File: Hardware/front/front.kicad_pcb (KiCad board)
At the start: 4 copper layers, 75 x 60 mm, 55 parts, among them J101 Conn_02x10_Odd_Even, SW101 Alps EC11E, SW102 C&K-D6R-Illuminated, SW103 B3W-9002-Y1C, SW104 B3W-9002-Y1C, SW105 B3W-9002-Y1C, SW106 B3W-9002-Y1C, SW107 B3W-9000-RHG2C, U101 XRA1203, U102 AT24CS32-SSHM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

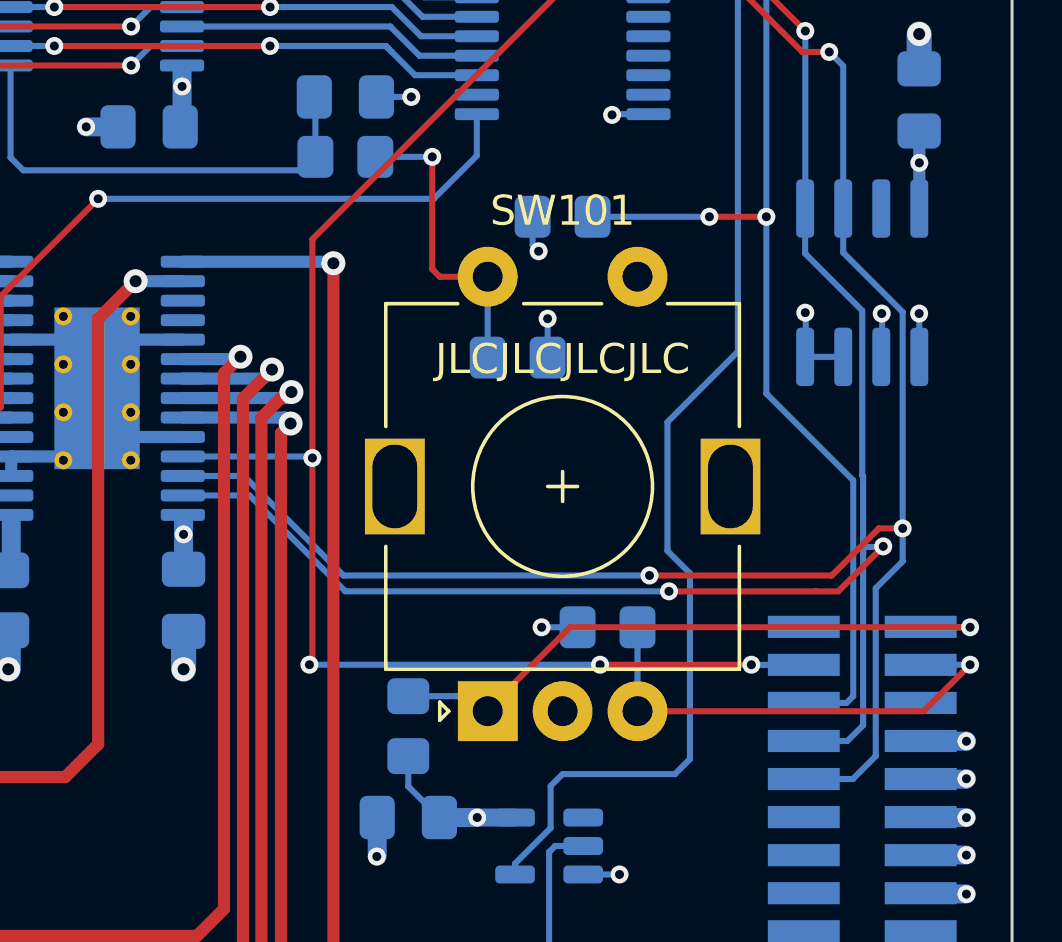
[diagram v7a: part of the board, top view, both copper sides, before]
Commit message: Changed front panel rotary encoder
- Switched the Alps encoder for a part that's a quarter the price, and
  also uses gray code rather than quadrature encoding. This is a bit
  more ubiquitous and easier to parse
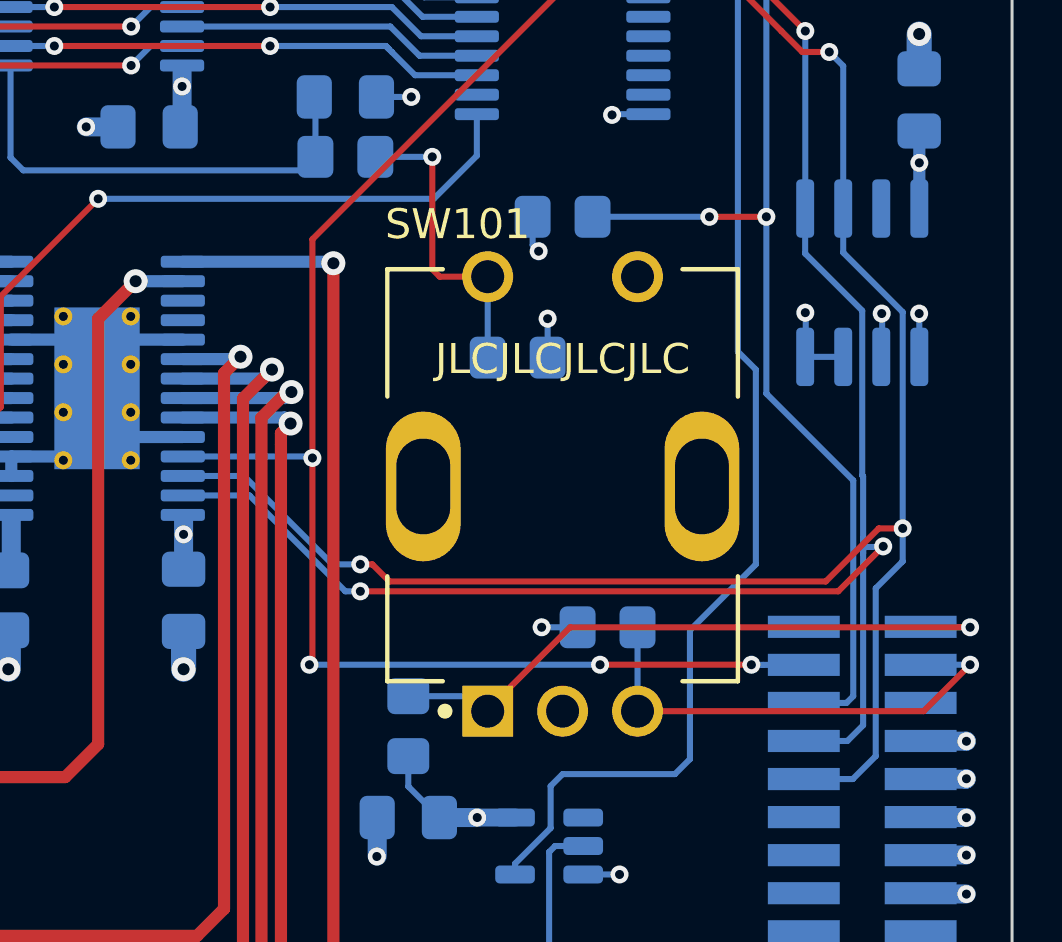
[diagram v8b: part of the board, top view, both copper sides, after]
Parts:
- SW101: value Alps EC11E -> TT EN11; footprint Rotary_Encoder:RotaryEncoder_Alps_EC11E-Switch_Vertical_H20mm -> programmable-load:TT_Electronics-EN11-HSM1AF15-0
- moved SW101 7.91 mm to (75.0, 43.0), turned to 0 degrees
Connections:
- R113 pad 1: Net-(R113-Pad1) -> Net-(SW101-PadS1)
- R114 pad 1: Net-(R113-Pad1) -> Net-(SW101-PadS1)
- SW101 pad S1: GND -> Net-(SW101-PadS1)
- SW101 pad S2: Net-(R113-Pad1) -> GND
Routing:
- net Net-(SW101-PadS1): track 0.00 -> 10.3 mm, vias 0 -> 1
- net Net-(R113-Pad1): track 10.3 -> 0.00 mm, vias 1 -> 0
